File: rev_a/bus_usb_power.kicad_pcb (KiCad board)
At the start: 2 copper layers, 50 x 50 mm, 18 parts, among them J1 TERMINATE_JUMPER, Q1 FQP47P06, Q2 FQP47P06, SW1 F-426-0020

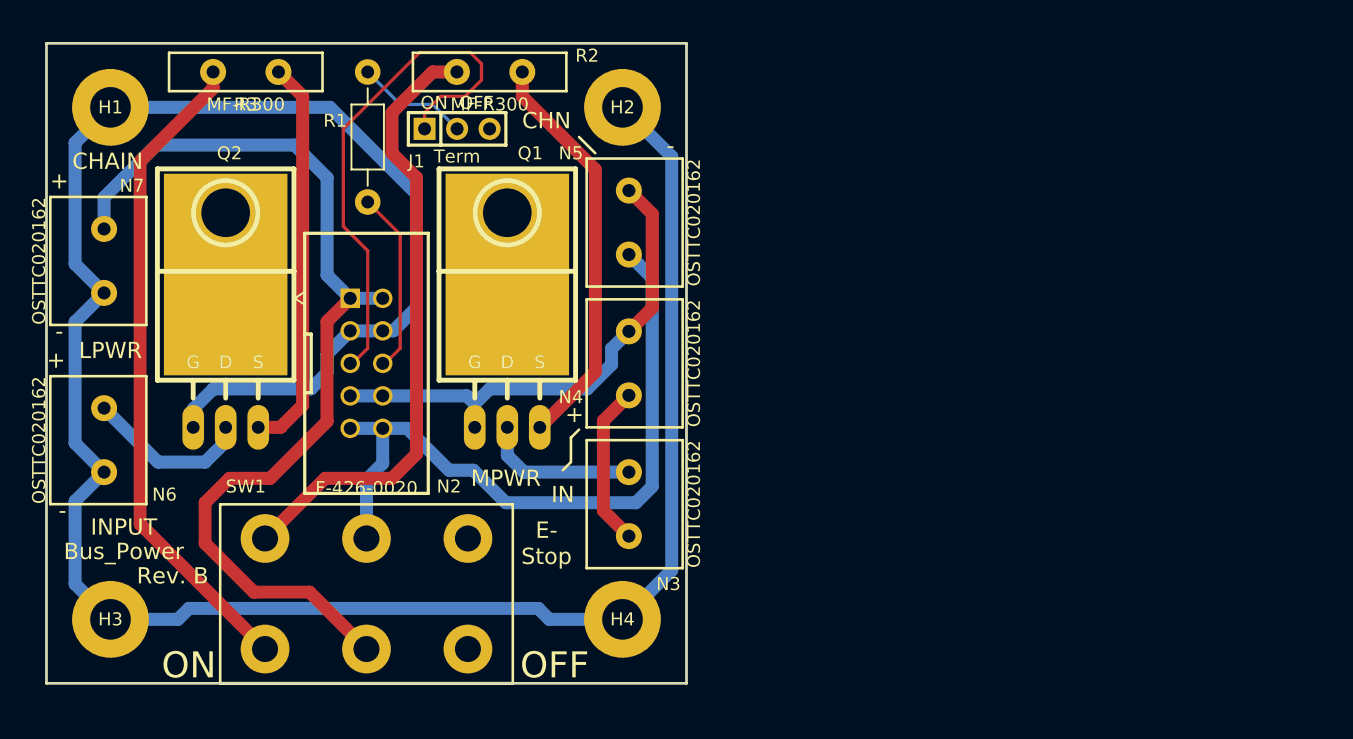
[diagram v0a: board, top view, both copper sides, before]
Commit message: Changed internal references from bus_power to bus_usb_power.
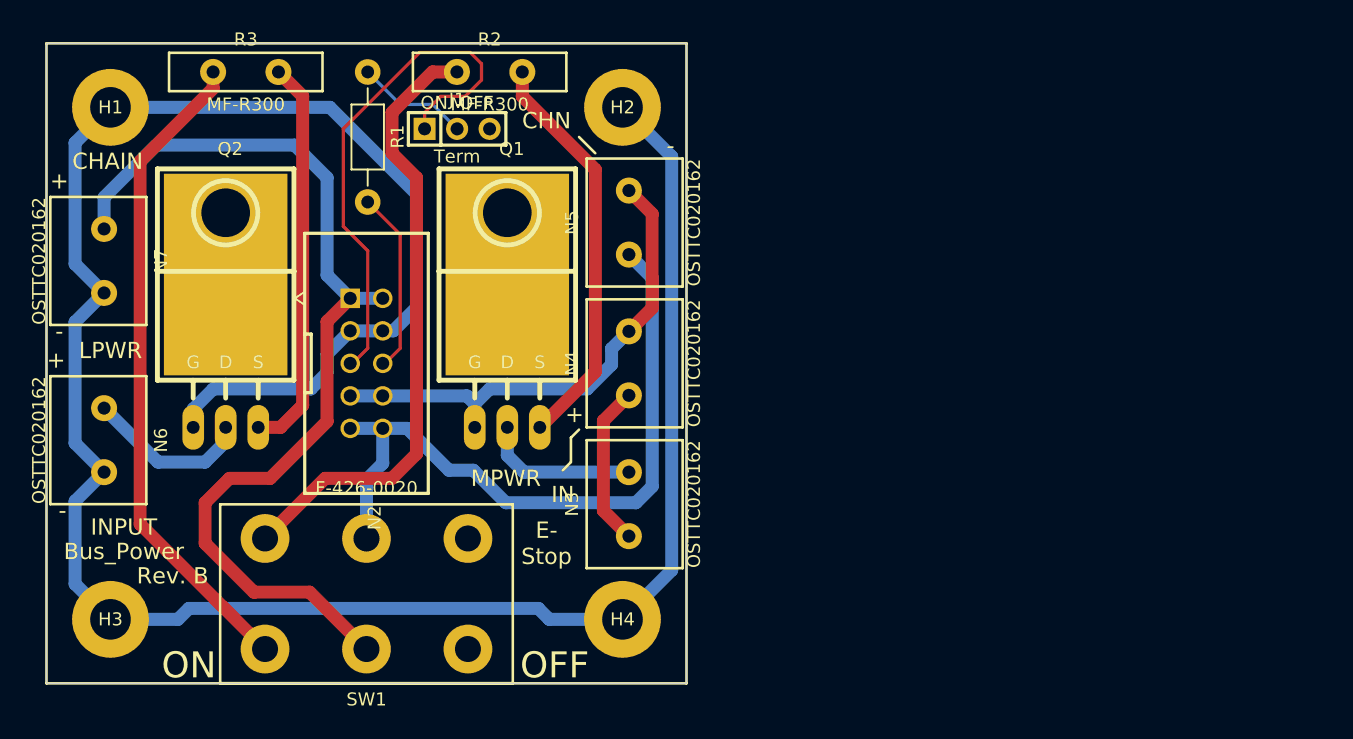
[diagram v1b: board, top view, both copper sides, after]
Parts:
- G1: footprint Bus_Power:OSHW_LOGO_400mil -> Bus_Usb_Power:OSHW_LOGO_400mil
- H1, H2, H3, H4: footprint Bus_Power:MountingHole_3mm -> Bus_Usb_Power:MountingHole_3mm
- J1: footprint Bus_Power:Pin_Header_Straight_1x03 -> Bus_Usb_Power:Pin_Header_Straight_1x03
- N2: footprint Bus_Power:Pin_Header_Straight_2x05_Shrouded -> Bus_Usb_Power:Pin_Header_Straight_2x05_Shrouded
- N3, N4, N5, N6, N7: footprint Bus_Power:5MM_TERMINAL_BLOCK_2_POS -> Bus_Usb_Power:5MM_TERMINAL_BLOCK_2_POS
- Q1, Q2: footprint Bus_Power:TO-220_FET-GDS_Horizontal_LargePads -> Bus_Usb_Power:TO-220_FET-GDS_Horizontal_LargePads
- R1: footprint Bus_Power:Resistor_Horizontal_400 -> Bus_Usb_Power:Resistor_Horizontal_400
- R2, R3: footprint Bus_Power:MF_R300 -> Bus_Usb_Power:MF_R300
- SW1: footprint Bus_Power:GF_426_0020 -> Bus_Usb_Power:GF_426_0020

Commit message: Initial layout of Rev. A is complete.
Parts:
- added N1: AY-Y1008-2-R, Bus_Usb_Power:DUAL_USB_A, F.Cu at (120.0, 113.7)
- added N8: AY-Y1008-2-R, Bus_Usb_Power:DUAL_USB_A, F.Cu at (137.8, 113.7)
- added R4: 200, Bus_Usb_Power:Resistor_Horizontal_400, F.Cu at (157.5, 127.6)
- added R5: 200, Bus_Usb_Power:Resistor_Horizontal_400, F.Cu at (157.5, 122.6)
- added R6: 200, Bus_Usb_Power:Resistor_Horizontal_400, F.Cu at (157.5, 117.5)
- added R7: 200, Bus_Usb_Power:Resistor_Horizontal_400, F.Cu at (157.5, 112.4)
- added VR1: D24V25F6, Bus_Usb_Power:D24V25F6, F.Cu at (126.4, 135.9)
- added VR2: OKI-78SR-5/1.5-W36-C, Bus_Usb_Power:OKI_DC_TO_DC_CONNECTOR, F.Cu at (137.8, 121.9)
- added VR3: OKI-78SR-5/1.5-W36-C, Bus_Usb_Power:OKI_DC_TO_DC_CONNECTOR, F.Cu at (120.0, 121.9)
- N3, N4, N5, N6, N7: value OSTTC020162 -> 2POS_5MM_TERM_BLK
- moved N7 93.2 mm to (196.2, 133.3)
- moved N6 92.6 mm to (196.2, 118.1)
- moved R3 74.7 mm to (179.1, 141.6)
- moved Q2 74.7 mm to (188.6, 133.3), turned to 90 degrees
- moved H2 50.0 mm to (195.0, 105.0)
- moved H4 50.0 mm to (195.0, 145.0)
- moved N3 49.5 mm to (182.9, 103.5), turned to 180 degrees
- moved R2 44.2 mm to (172.1, 125.7)
- moved J1 39.2 mm to (114.3, 141.6), turned to 270 degrees
- moved Q1 35.8 mm to (169.5, 117.5), turned to 270 degrees
- moved N4 31.8 mm to (168.9, 103.5), turned to 180 degrees
- moved SW1 27.4 mm to (152.4, 142.9)
- moved R1 25.9 mm to (114.3, 130.8), turned to 90 degrees
- moved N2 19.6 mm to (105.4, 125.7)
- moved G1 16.6 mm to (123.8, 131.4), turned to 180 degrees
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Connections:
- J1 pad 3: Net-(J1-Pad3) -> (no net)
- N2 pad 1: /LPWR4 -> /LPWR5
- N2 pad 2: /LPWR4 -> /LPWR5
- N5 pad 2: /MPWR4 -> /MPWR0
- N7 pad 2: /LPWR4 -> /LPWR1
- SW1 pad 3: Net-(SW1-Pad3) -> (no net)
- SW1 pad 4: /LPWR3 -> /LPWR4
- SW1 pad 5: /LPWR4 -> /LPWR5
- SW1 pad 6: Net-(SW1-Pad6) -> (no net)
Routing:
- net /MGND: track 39.4 -> 184.3 mm
- net Net-(N1-Pad2): track 0.00 -> 71.0 mm
- net /LPWR5: track 0.00 -> 70.9 mm, vias 0 -> 1
- net Net-(N1-Pad3): track 0.00 -> 65.4 mm
- net Net-(N1-Pad7): track 0.00 -> 46.2 mm
- net Net-(N1-Pad6): track 0.00 -> 37.0 mm
- net Net-(N8-Pad3): track 0.00 -> 30.9 mm
- net Net-(N8-Pad7): track 0.00 -> 28.5 mm
- net /MPWR2: track 31.9 -> 8.58 mm
- net Net-(J1-Pad1): track 41.5 -> 18.7 mm
- net Net-(N8-Pad2): track 0.00 -> 22.3 mm
- net Net-(N8-Pad6): track 0.00 -> 21.9 mm
- net /LPWR4: track 77.1 -> 55.4 mm
- net /MPWR0: track 12.6 -> 32.1 mm
- net /MPWR1: track 12.2 -> 29.5 mm
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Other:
- board size 50 x 50 mm -> 100 x 50 mm
- board text added: "1"
- board text added: "Bus USB Power Rev. A 10Jan2015 (c) Gramlich"
- board text added: "Bus_USB_Power"
- board text added: "E-STOP"
- board text added: "Rev. A 10Jan2015"
- board text removed: "Bus Power Rev. B 1Oct2014 (c) Gramlich"
- board text removed: "Bus_Power"
- board text removed: "CHN"
- board text removed: "E- Stop"
- board text removed: "ON OFF"
- board text removed: "Rev. B"

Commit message: Rev A. read for manufacture.
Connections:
- H1 pad 1: /LGND -> (no net)
- H2 pad 1: /LGND -> (no net)
- H3 pad 1: /LGND -> (no net)
- H4 pad 1: /LGND -> (no net)
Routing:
- net /LGND: track 196.5 -> 142.0 mm
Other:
- board text added: "Bus USB Power Rev. A 13Jan2015 (c) Gramlich"
- board text added: "Rev. A 13Jan2015"
- board text removed: "Bus USB Power Rev. A 10Jan2015 (c) Gramlich"
- board text removed: "Rev. A 10Jan2015"
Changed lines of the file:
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@@
 (kicad_pcb (version 4) (host pcbnew "(2014-jul-16 BZR unknown)-product")
   (general
-    (links 62)
+    (links 58)
     (no_connects 0)
-    (area 90.498972 83.0072 204.052714 150.3568)
+    (area 90.498972 98.4712 200.101601 150.3568)
     (thickness 1.6)
     (drawings 39)
-    (tracks 196)
+    (tracks 188)
     (zones 0)
     (modules 27)
@@
     (mod_text_size 1 1)
     (mod_text_width 0.15)
-    (pad_size 1.7272 1.7272)
-    (pad_drill 1.016)
+    (pad_size 6 6)
+    (pad_drill 3.175)
     (pad_to_mask_clearance 0)
     (aux_axis_origin 0 0)
@@
     )
     (fp_circle (center 0 0) (end 3 0) (layer Cmts.User) (width 0.381))
-    (pad 1 thru_hole circle (at 0 0) (size 6 6) (drill 3.175) (layers *.Cu *.SilkS)
-      (net 5 /LGND))
+    (pad 1 thru_hole circle (at 0 0) (size 6 6) (drill 3.175) (layers *.Cu *.SilkS))
   )
   (module Bus_Usb_Power:MountingHole_3mm (layer F.Cu)
@@
     )
     (fp_circle (center 0 0) (end 3 0) (layer Cmts.User) (width 0.381))
-    (pad 1 thru_hole circle (at 0 0) (size 6 6) (drill 3.175) (layers *.Cu *.SilkS)
-      (net 5 /LGND))
+    (pad 1 thru_hole circle (at 0 0) (size 6 6) (drill 3.175) (layers *.Cu *.SilkS))
   )
   (module Bus_Usb_Power:MountingHole_3mm (layer F.Cu)
@@
     )
     (fp_circle (center 0 0) (end 3 0) (layer Cmts.User) (width 0.381))
-    (pad 1 thru_hole circle (at 0 0) (size 6 6) (drill 3.175) (layers *.Cu *.SilkS)
-      (net 5 /LGND))
+    (pad 1 thru_hole circle (at 0 0) (size 6 6) (drill 3.175) (layers *.Cu *.SilkS))
   )
   (module Bus_Usb_Power:MountingHole_3mm (layer F.Cu)
@@
     )
     (fp_circle (center 0 0) (end 3 0) (layer Cmts.User) (width 0.381))
-    (pad 1 thru_hole circle (at 0 0) (size 6 6) (drill 3.175) (layers *.Cu *.SilkS)
-      (net 5 /LGND))
+    (pad 1 thru_hole circle (at 0 0) (size 6 6) (drill 3.175) (layers *.Cu *.SilkS))
   )
   (module Bus_Usb_Power:Pin_Header_Straight_1x03 (layer F.Cu)
@@
   (gr_line (start 100 150) (end 200 150) (angle 90) (layer Edge.Cuts) (width 0.1))
   (gr_line (start 100 100) (end 100 150) (angle 90) (layer Edge.Cuts) (width 0.1))
-  (gr_text "Bus USB Power Rev. A\n10Jan2015\n(c) Gramlich" (at 129.794 104.14) (layer B.SilkS)
+  (gr_text "Bus USB Power Rev. A\n13Jan2015\n(c) Gramlich" (at 129.794 104.14) (layer B.SilkS)
     (effects (font (size 1.27 1.27) (thickness 0.2032)) (justify mirror))
   )
@@
     (effects (font (thickness 0.254)) (justify mirror))
   )
-  (gr_text "Rev. A 10Jan2015" (at 144.78 132.08) (layer F.SilkS)
+  (gr_text "Rev. A 13Jan2015" (at 144.78 132.08) (layer F.SilkS)
     (effects (font (size 1.27 1.27) (thickness 0.2032)))
   )
@@
   (segment (start 193.675 118.15) (end 193.675 128.31) (width 1.016) (layer F.Cu) (net 1))
   (segment (start 176.5173 141.605) (end 172.466 141.605) (width 1.016) (layer B.Cu) (net 2))
-  (segment (start 139.192 142.748) (end 135.89 146.05) (width 1.016) (layer B.Cu) (net 2))
-  (segment (start 171.323 142.748) (end 139.192 142.748) (width 1.016) (layer B.Cu) (net 2))
-  (segment (start 172.466 141.605) (end 171.323 142.748) (width 1.016) (layer B.Cu) (net 2))
+  (segment (start 139.7 142.24) (end 135.89 146.05) (width 1.016) (layer B.Cu) (net 2))
+  (segment (start 171.831 142.24) (end 139.7 142.24) (width 1.016) (layer B.Cu) (net 2))
+  (segment (start 172.466 141.605) (end 171.831 142.24) (width 1.016) (layer B.Cu) (net 2))
   (segment (start 133.35 146.05) (end 135.89 146.05) (width 1.016) (layer B.Cu) (net 2))
   (segment (start 188.595 130.81) (end 190.5 130.81) (width 1.016) (layer F.Cu) (net 3))
@@
   (segment (start 141.478 147.193) (end 137.795 143.51) (width 1.016) (layer F.Cu) (net 4))
   (segment (start 106.68 123.19) (end 104.14 123.19) (width 1.016) (layer B.Cu) (net 5))
-  (segment (start 104.14 123.19) (end 101.6 123.19) (width 1.016) (layer F.Cu) (net 5))
-  (segment (start 105 145) (end 101.6 141.6) (width 1.016) (layer F.Cu) (net 5))
-  (segment (start 101.6 108.4) (end 105 105) (width 1.016) (layer F.Cu) (net 5))
-  (segment (start 101.6 141.6) (end 101.6 123.19) (width 1.016) (layer F.Cu) (net 5))
-  (segment (start 101.6 123.19) (end 101.6 108.4) (width 1.016) (layer F.Cu) (net 5))
+  (segment (start 137.16 148.59) (end 141.605 144.145) (width 1.016) (layer B.Cu) (net 5))
   (segment (start 130.81 146.05) (end 133.35 148.59) (width 1.016) (layer B.Cu) (net 5))
-  (segment (start 167.225 145) (end 195 145) (width 1.016) (layer B.Cu) (net 5))
-  (segment (start 166.37 144.145) (end 167.225 145) (width 1.016) (layer B.Cu) (net 5))
-  (segment (start 141.605 144.145) (end 166.37 144.145) (width 1.016) (layer B.Cu) (net 5))
-  (segment (start 137.16 148.59) (end 141.605 144.145) (width 1.016) (layer B.Cu) (net 5))
   (segment (start 133.35 148.59) (end 137.16 148.59) (width 1.016) (layer B.Cu) (net 5))
-  (segment (start 105 145) (end 108.59 148.59) (width 1.016) (layer B.Cu) (net 5))
   (segment (start 128.27 148.59) (end 130.81 146.05) (width 1.016) (layer B.Cu) (net 5))
-  (segment (start 108.59 148.59) (end 128.27 148.59) (width 1.016) (layer B.Cu) (net 5))
+  (segment (start 114.935 148.59) (end 128.27 148.59) (width 1.016) (layer B.Cu) (net 5))
   (segment (start 188.595 135.89) (end 196.175 135.89) (width 1.016) (layer B.Cu) (net 5))
   (segment (start 196.175 135.89) (end 196.215 135.85) (width 1.016) (layer B.Cu) (net 5))
-  (segment (start 195 145) (end 195 137.065) (width 1.016) (layer F.Cu) (net 5))
-  (segment (start 195 137.065) (end 196.215 135.85) (width 1.016) (layer F.Cu) (net 5))
   (segment (start 196.215 120.61) (end 198.755 123.15) (width 1.016) (layer F.Cu) (net 5))
   (segment (start 198.755 133.31) (end 196.215 135.85) (width 1.016) (layer F.Cu) (net 5))
   (segment (start 198.755 123.15) (end 198.755 133.31) (width 1.016) (layer F.Cu) (net 5))
-  (segment (start 196.215 120.61) (end 198.755 118.07) (width 1.016) (layer F.Cu) (net 5))
-  (segment (start 198.755 108.755) (end 195 105) (width 1.016) (layer F.Cu) (net 5))
-  (segment (start 198.755 118.07) (end 198.755 108.755) (width 1.016) (layer F.Cu) (net 5))
+  (segment (start 188.595 135.89) (end 188.595 138.43) (width 1.016) (layer B.Cu) (net 5))
+  (segment (start 182.88 144.145) (end 188.595 138.43) (width 1.016) (layer B.Cu) (net 5))
+  (segment (start 141.605 144.145) (end 182.88 144.145) (width 1.016) (layer B.Cu) (net 5))
+  (segment (start 101.6 125.73) (end 101.6 135.255) (width 1.016) (layer B.Cu) (net 5))
+  (segment (start 101.6 135.255) (end 114.935 148.59) (width 1.016) (layer B.Cu) (net 5))
+  (segment (start 104.14 123.19) (end 101.6 125.73) (width 1.016) (layer B.Cu) (net 5))
   (segment (start 114.3 141.605) (end 116.205 139.7) (width 0.254) (layer F.Cu) (net 6))
   (segment (start 116.205 137.795) (end 114.3 135.89) (width 0.254) (layer F.Cu) (net 6))
